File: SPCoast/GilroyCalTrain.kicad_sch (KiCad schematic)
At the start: 94 parts, among them SW3771 771, SW3773 773, SW3775 775

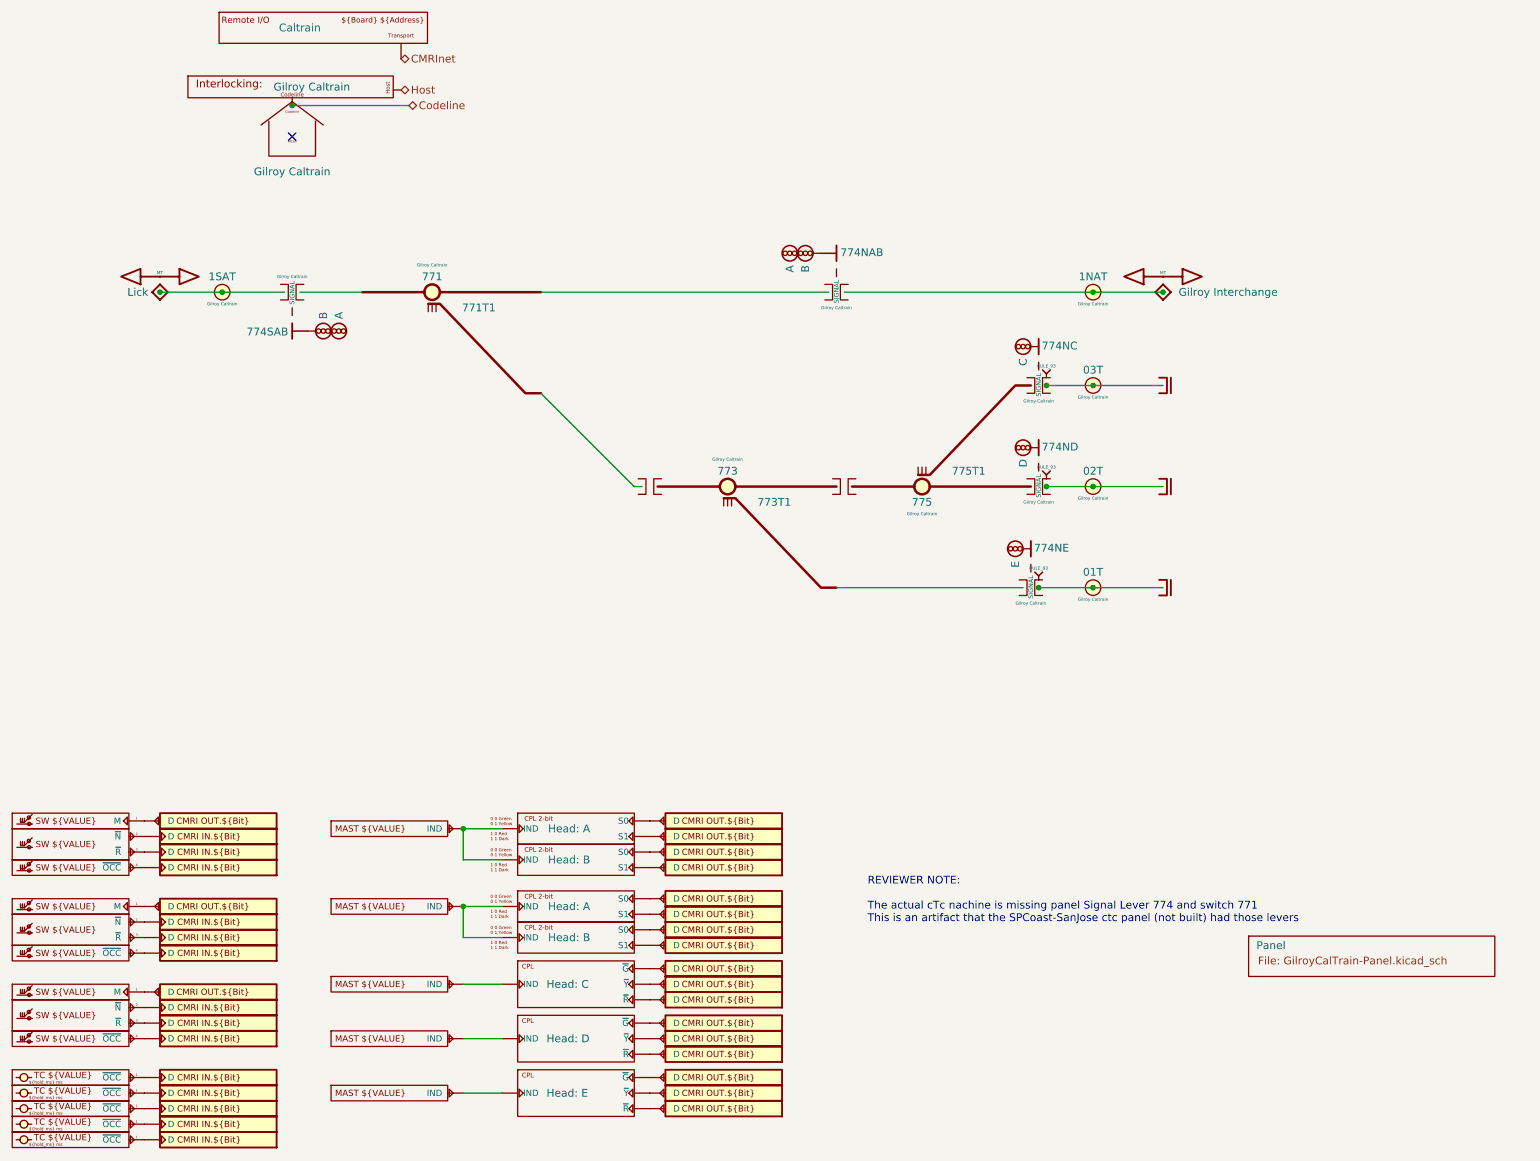
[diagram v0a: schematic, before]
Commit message: chore(kicad): owner edits: uniform unit ports Codeline, Host, IOBus, OfficeIOBus; panels on the desk bus
Owner's edits, committed as they stand (2026-10-21): every unit sheet exposes the same four
ports and the parent wires only the ones it needs; Caltrain's and Interchange's panels reach
the desk bus through OfficeIOBus; unused ports carry no-connect flags; grid snaps fixed.
Two label spellings are still mismatched (Luchessa's OfficeIOBus vs the root's OfficeBusIO;
Interchange's JMRI_MQTT vs the root's IOBus), fixed in the next commit.
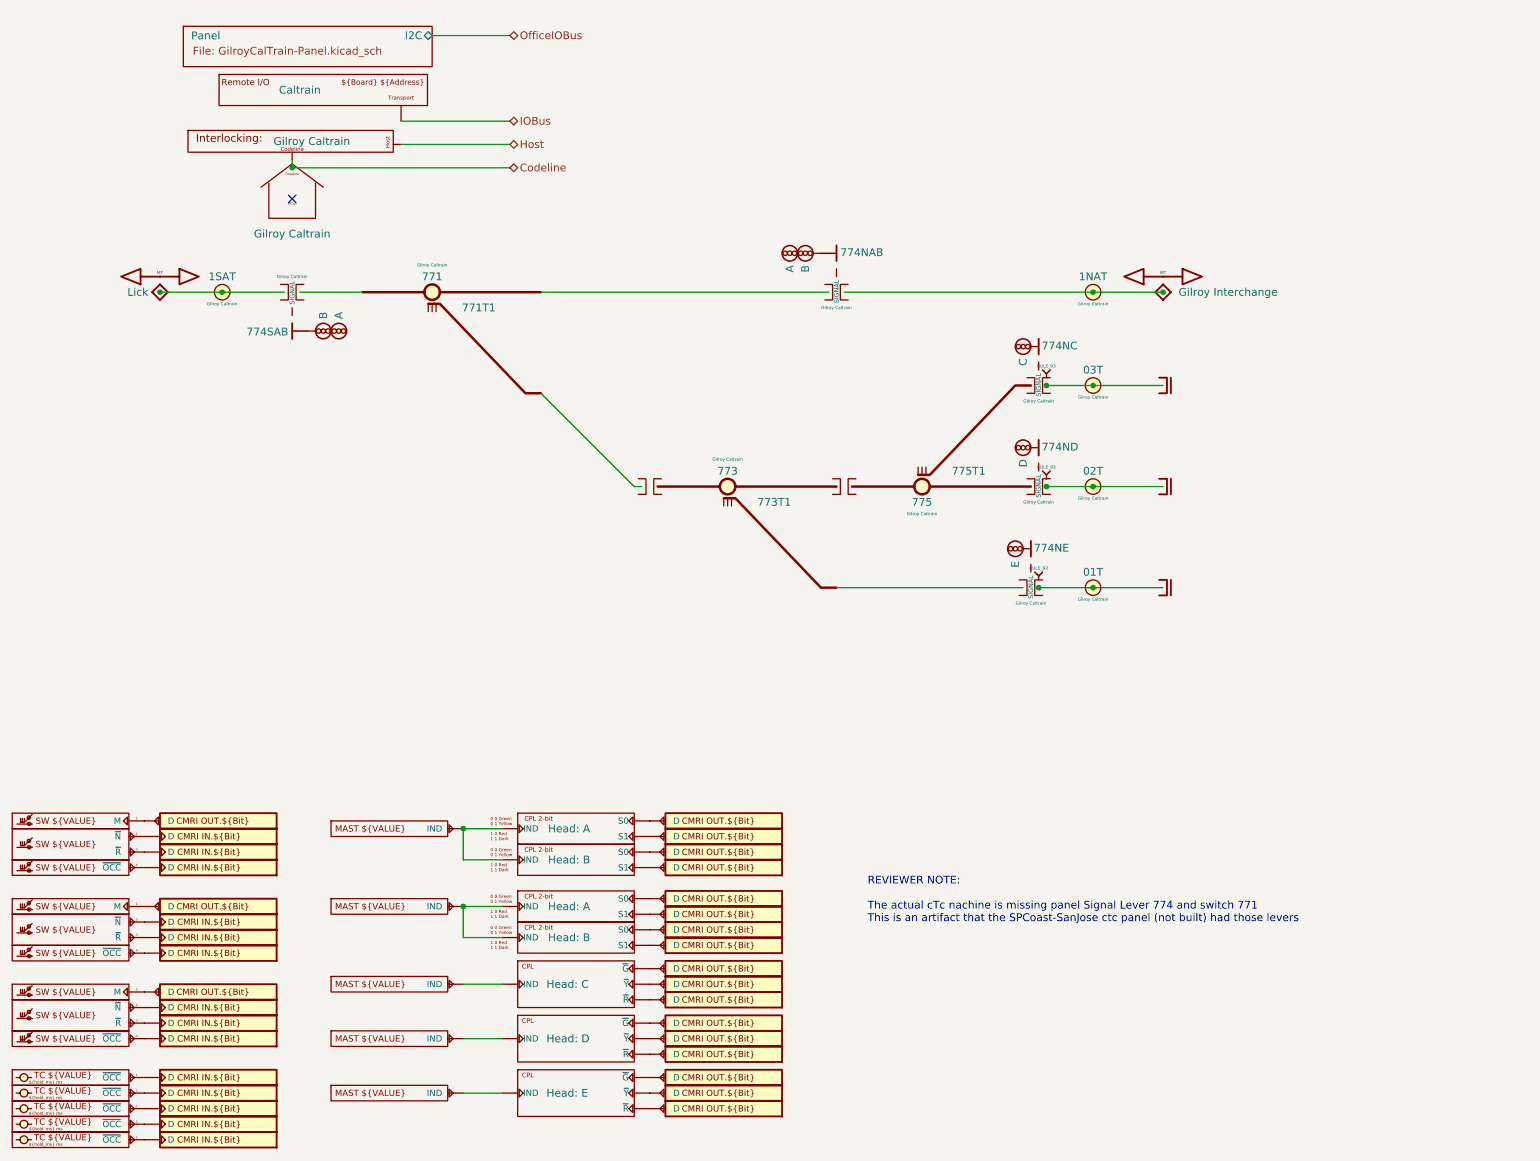
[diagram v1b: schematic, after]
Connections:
- net CMRInet renamed IOBus
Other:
- sheet Panel ports: added I2C; removed none
